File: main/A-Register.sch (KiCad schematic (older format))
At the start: 19 parts, among them U1 74LS245, U2 74LS173, U3 74LS173

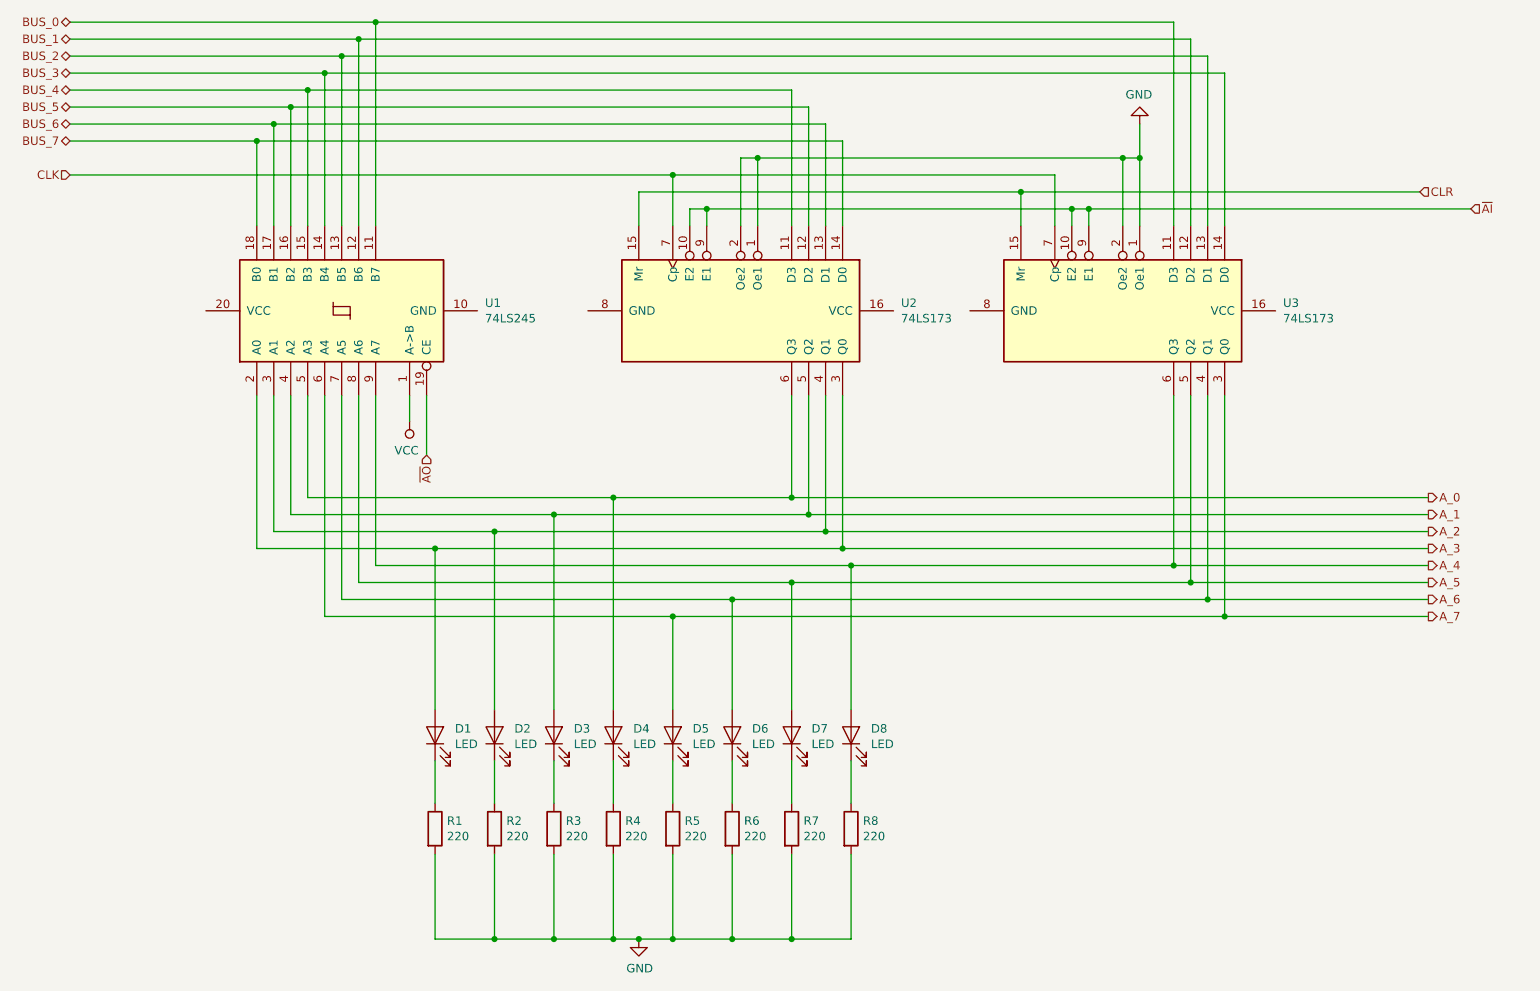
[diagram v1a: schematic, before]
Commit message: Switch to using 74LS377 in place of two 74LS173
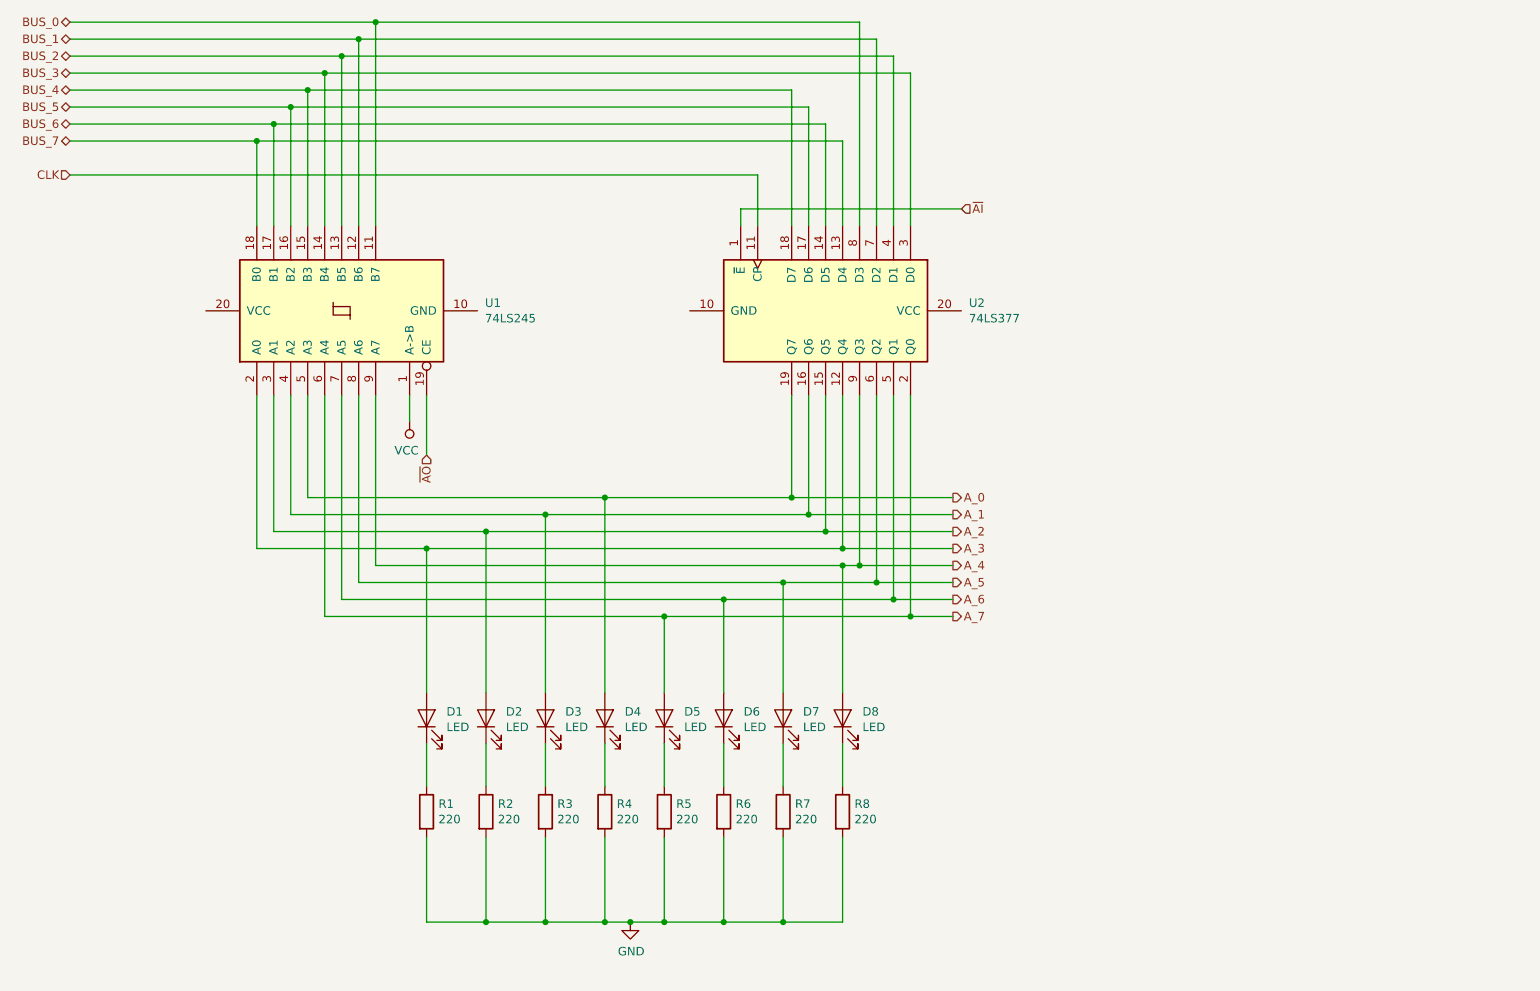
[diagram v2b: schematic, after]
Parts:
- removed U2, U3: 74LS173, symbol 74xx:74LS173
- added U2: 74LS377, symbol 74xx:74LS377
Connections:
- net A_0: now also U2.19 (Q7)
- net A_1: now also U2.16 (Q6)
- net A_2: now also U2.15 (Q5)
- net A_3: now also U2.12 (Q4)
- net A_4: now also U2.9 (Q3)
- net A_5: now also U2.6 (Q2)
- net A_6: now also U2.5 (Q1)
- net A_7: now also U2.2 (Q0)
- net BUS_0: now also U2.8 (D3)
- net BUS_1: now also U2.7 (D2)
- net BUS_2: now also U2.4 (D1)
- net BUS_3: now also U2.3 (D0)
- net BUS_4: now also U2.18 (D7)
- net BUS_5: now also U2.17 (D6)
- net BUS_6: now also U2.14 (D5)
- net BUS_7: now also U2.13 (D4)
- net CLK: now also U2.11 (CP)
- net ~AI~: now also U2.1 (~E)
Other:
- moved on the sheet: D1, D2, D3, D4, D5, D6, D7, D8, R1, R2, R3, R4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
